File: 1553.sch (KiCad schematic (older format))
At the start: 20 parts

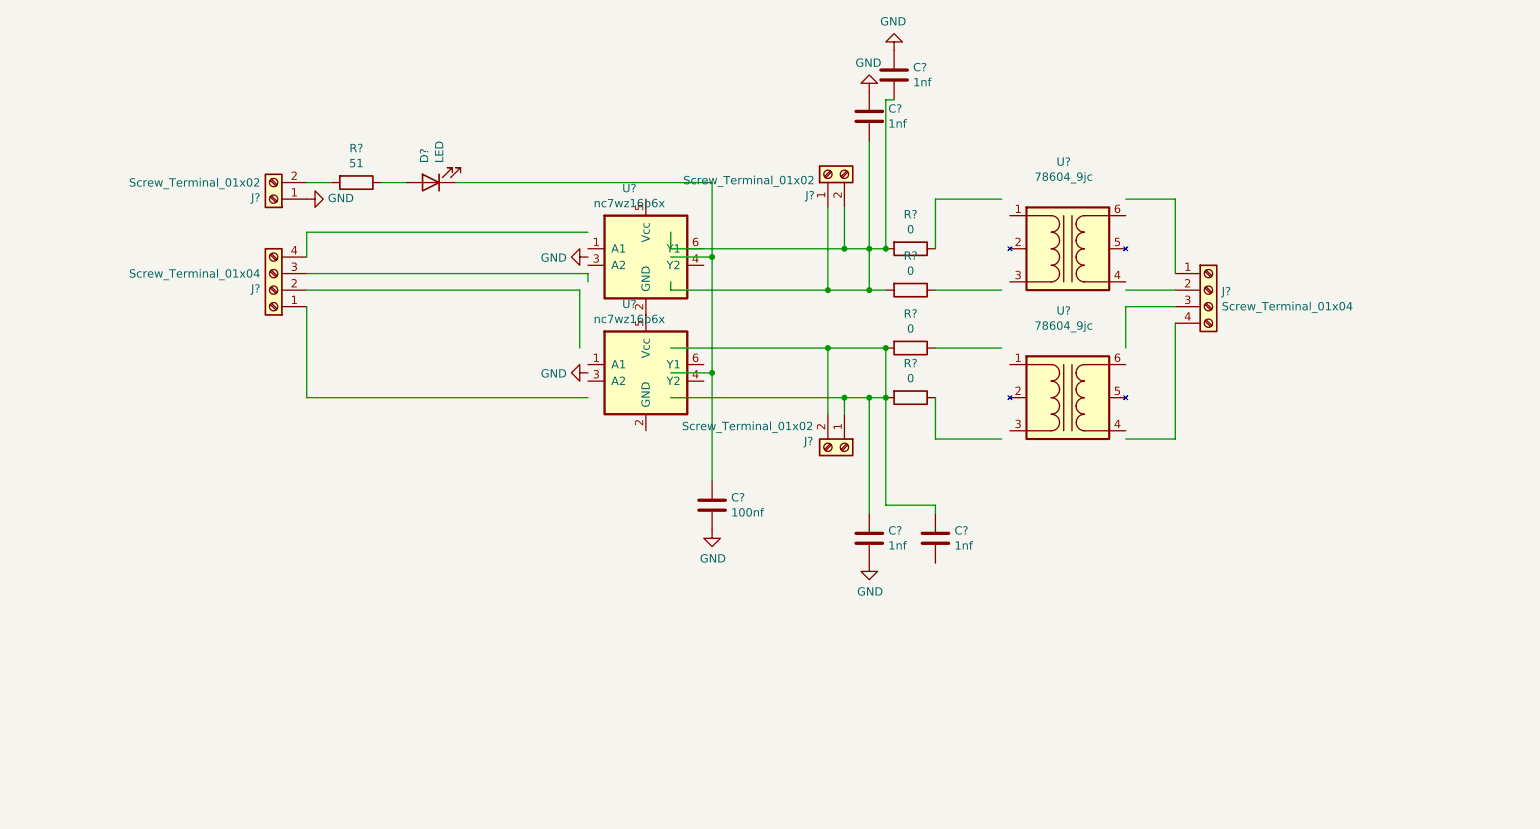
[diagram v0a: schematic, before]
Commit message: update schematic, and perform initial layout.
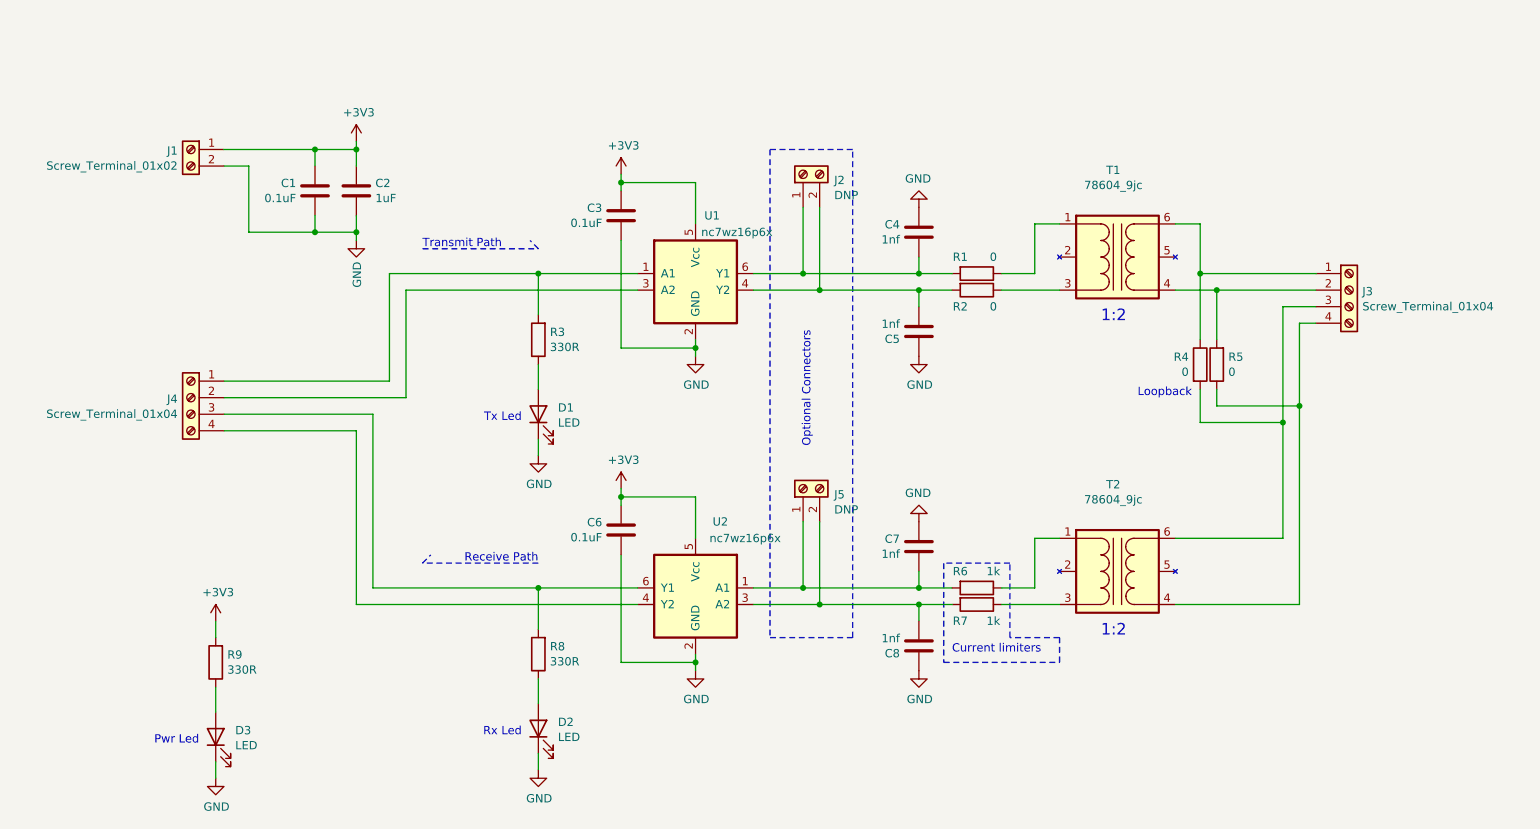
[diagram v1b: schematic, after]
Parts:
- removed C?: 100nf, symbol Device:C
- removed C? (x2): 1nf, symbol Device:C
- removed J?: Screw_Terminal_01x02, symbol Connector:Screw_Terminal_01x02
- removed R? (x2): 0, symbol Device:R
- removed U?: 78604_9jc, symbol 1553:78604_9jc
- removed U? (x2): nc7wz16p6x, symbol 1553:nc7wz16p6x
- added C1, C3, C6: 0.1uF, Capacitor_SMD:C_0603_1608Metric, symbol Device:C
- added C2: 1uF, Capacitor_SMD:C_0603_1608Metric, symbol Device:C
- added C7, C8: 1nf, Capacitor_SMD:C_0603_1608Metric, symbol Device:C
- added D1, D2: LED, LED_SMD:LED_0603_1608Metric, symbol Device:LED
- added J5: DNP, TerminalBlock_TE-Connectivity:TerminalBlock_TE_282834-2_1x02_P2.54mm_Horizontal, symbol Connector:Screw_Terminal_01x02
- added R3, R8: 330R, Resistor_SMD:R_0603_1608Metric, symbol Device:R
- added R4, R5: 0, Resistor_SMD:R_0603_1608Metric, symbol Device:R
- added R6, R7: 1k, Resistor_SMD:R_0603_1608Metric, symbol Device:R
- added T2: 78604_9jc, 1553-addon:786J, symbol 1553:78604_9jc
- added U1, U2: nc7wz16p6x, Package_TO_SOT_SMD:SOT-363_SC-70-6, symbol 1553:nc7wz16p6x
- C4, C5: renamed from C?; footprint (none) -> Capacitor_SMD:C_0603_1608Metric; Mfg (none) -> Yageo; PN (none) -> CC0603JRNPO9BN102
- D3: renamed from D?; footprint (none) -> LED_SMD:LED_0603_1608Metric; Mfg (none) -> Lite-On Inc.; PN (none) -> LTST-C191KSKT
- J1: renamed from J?; footprint (none) -> TerminalBlock_TE-Connectivity:TerminalBlock_TE_282834-2_1x02_P2.54mm_Horizontal; Mfg (none) -> TE Connectivity AMP Connectors; PN (none) -> 282834-2
- J2: renamed from J?; value Screw_Terminal_01x02 -> DNP; footprint (none) -> TerminalBlock_TE-Connectivity:TerminalBlock_TE_282834-2_1x02_P2.54mm_Horizontal; Mfg (none) -> TE Connectivity AMP Connectors; PN (none) -> 282834-2
- J3, J4: renamed from J?; footprint (none) -> TerminalBlock_TE-Connectivity:TerminalBlock_TE_282834-4_1x04_P2.54mm_Horizontal; Mfg (none) -> TE Connectivity AMP Connectors; PN (none) -> 282834-4
- R1, R2: renamed from R?; footprint (none) -> Resistor_SMD:R_0603_1608Metric; Mfg (none) -> Yageo; PN (none) -> RC0603JR-070RL
- R9: renamed from R?; value 51 -> 330R; footprint (none) -> Resistor_SMD:R_0603_1608Metric; Mfg (none) -> Yageo; PN (none) -> RC0603FR-07330RL
- T1: renamed from U?; footprint (none) -> 1553-addon:786J; Mfg (none) -> Murata Power Solutions Inc.; PN (none) -> 78604/9JC
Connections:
- net labels added: +3V3
- wire segments 55 -> 98
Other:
- note added: "1:2"
- note added: "Current limiters"
- note added: "Loopback"
- note added: "Optional Connectors"
- note added: "Pwr Led"
- note added: "Receive Path"
- note added: "Rx Led"
- note added: "Transmit Path"
- note added: "Tx Led"
- moved on the sheet: C4, C5, D3, J1, J2, J3, J4, R1, R2, R9, T1
